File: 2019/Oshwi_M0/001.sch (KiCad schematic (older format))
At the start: 101 parts, among them CN1 MICROSD, CN2 MicroB USB, IC1 APX803, J1 Conn_01x01, J10 Conn_01x01, J11 Conn_01x01, J12 Conn_01x01, J13 Conn_01x01, J14 Conn_01x01, J15 Conn_01x01, J16 Conn_01x01, J17 Conn_01x01, J18 Conn_01x01, J19 Conn_01x01, J2 Conn_01x01, J20 Conn_01x01, J21 Conn_01x01, J22 Conn_01x01, J23 Conn_01x01, J24 USB_MICRO, J26 Micro_SD_Card_Det, J3 Conn_01x01, J4 Conn_01x01, J5 Conn_01x01, J6 Conn_01x01, J7 Conn_01x01, J8 Conn_01x01, J9 Conn_01x01, Q1 MMBT2222, Q2 mmbt2222, SW1 SW_Push, SW2 EVQQ, SW3 EVQQ, U2 Memory_Flash, U3 ATSAMD21G18A-AUT, U5 DISP_LCD_0.9IN_160X80, U6 AP2112K-3.3, Y1 32.768

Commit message: Auto stash before merge of "master" and "origin/master"
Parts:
- removed 3.3VTAP1, 3V3TAP1, GND3TAP1, GNDTAP1, GNDTAP2, VCC1: SEWTAP-ALLIGATOR, Adafruit Circuit Playground Express:SEWALLI, symbol 001-rescue:SEWTAP-ALLIGATOR-Adafruit_Circuit_Playground_Express-eagle-import
- removed BATT1: 3-6VDC, Adafruit Circuit Playground Express:JSTPH2, symbol 001-rescue:CON_JST_PH_2PIN-Adafruit_Circuit_Playground_Express-eagle-import
- removed C11, C13, C14, C15: 1uF, Adafruit Circuit Playground Express:0603-NO, symbol 001-rescue:CAP_CERAMIC0603_NO-Adafruit_Circuit_Playground_Express-eagle-import
- removed C12, C8: 10uF, Adafruit Circuit Playground Express:0805-NO, symbol 001-rescue:CAP_CERAMIC0805-NOOUTLINE-Adafruit_Circuit_Playground_Express-eagle-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
- removed CN1: MICROSD, Adafruit 0.96in 160x80 TFT Display:MICROSD, symbol Adafruit_0.96in_160x80_TFT_Display-eagle-import:MICROSD
- removed CN2: MicroB USB, Adafruit Circuit Playground Express:4UCONN_20329_V2, symbol 001-rescue:USB_MICRO_20329_V2-Adafruit_Circuit_Playground_Express-eagle-import
- removed D4, D5: MBR120, Adafruit Circuit Playground Express:SOD-123, symbol 001-rescue:DIODESOD-123-Adafruit_Circuit_Playground_Express-eagle-import
- removed F1: 6V+ 500mA, Adafruit Circuit Playground Express:R1206, symbol 001-rescue:PTCFUSE-1206-Adafruit_Circuit_Playground_Express-eagle-import
- removed J26: Micro_SD_Card_Det, symbol 001-rescue:Micro_SD_Card_Det-conn
- removed U6: AP2112K-3.3, Adafruit Circuit Playground Express:SOT23-5, symbol 001-rescue:VREG_SOT23-5-Adafruit_Circuit_Playground_Express-eagle-import
- added X?: MICROSD, symbol oshwi_M0:MICROSD
- C? (x3): symbol device:C_Small -> 001-rescue:C_Small-device
- F2: symbol device:Polyfuse_Small -> 001-rescue:Polyfuse_Small-device
- J?: symbol conn:CONN_01X02 -> 001-rescue:CONN_01X02-conn
- R2, R6, R?: symbol device:R_Small -> 001-rescue:R_Small-device
- U?: symbol regul:AP2127K-3.3 -> 001-rescue:AP2127K-3.3-regul
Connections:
- wire segments 287 -> 247
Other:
- note removed: "3.3V Reg"
- note removed: "JST Battery In"
- note removed: "POWER SUPPLY"
- note removed: "USB Power/Data"

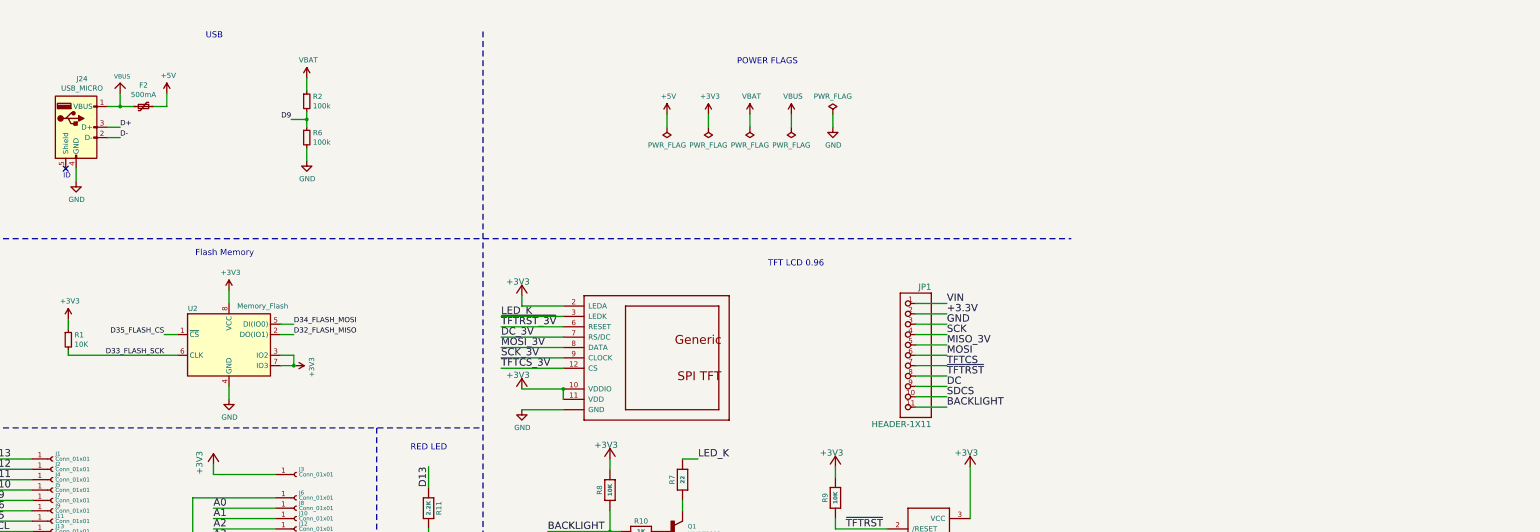
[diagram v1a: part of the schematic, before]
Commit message: Update Symbol MicroUSB
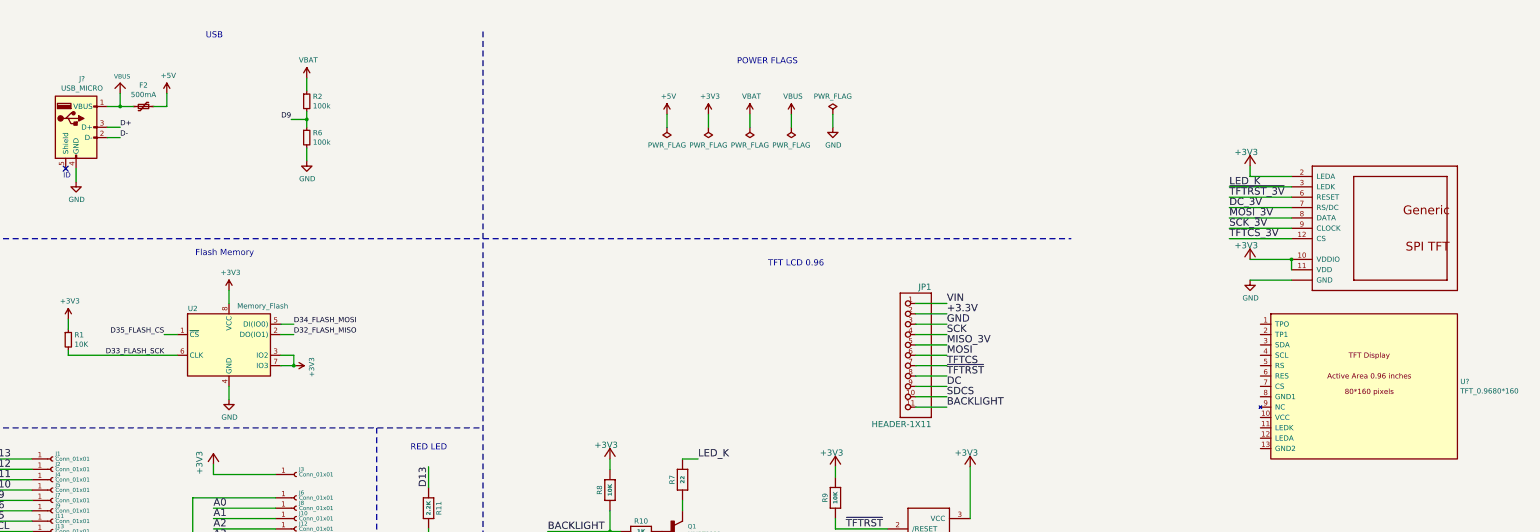
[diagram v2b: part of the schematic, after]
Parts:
- removed J24: USB_MICRO, symbol 001-rescue:USB_MICRO-oshwi_M0
- added J?: USB_MICRO, symbol oshwi_M0:USB_MICRO
- added U?: TFT_0.9680*160, symbol tft-shield:TFT_0.9680*160
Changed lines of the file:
@@
 L Adafruit_0.96in_160x80_TFT_Display-eagle-import:DISP_LCD_0.9IN_160X80 U5
 U 1 1 5CCCC118
-P 12725 3875
-F 0 "U5" H 12725 3875 50  0001 C CNN
-F 1 "DISP_LCD_0.9IN_160X80" H 12725 3875 50  0001 C CNN
-F 2 "Adafruit 0.96in 160x80 TFT Display:TFT_0.96IN_160X80" H 12725 3875 50  0001 C CNN
-F 3 "" H 12725 3875 50  0001 C CNN
-	1    12725 3875
+P 19750 2625
+F 0 "U5" H 19750 2625 50  0001 C CNN
+F 1 "DISP_LCD_0.9IN_160X80" H 19750 2625 50  0001 C CNN
+F 2 "Adafruit 0.96in 160x80 TFT Display:TFT_0.96IN_160X80" H 19750 2625 50  0001 C CNN
+F 3 "" H 19750 2625 50  0001 C CNN
+	1    19750 2625
 	1    0    0    -1
 $EndComp
@@
 Wire Wire Line
 	13325 7850 12425 7850
-Text Label 11025 3775 0    70   ~ 0
+Text Label 18050 2525 0    70   ~ 0
 MOSI_3V
 Wire Wire Line
-	11025 3775 11625 3775
+	18050 2525 18650 2525
 Text Label 12425 7650 0    70   ~ 0
 MOSI
@@
 Wire Wire Line
 	12775 5250 12775 5350
-Text Label 11025 3475 0    70   ~ 0
+Text Label 18050 2225 0    70   ~ 0
 LED_K
 Wire Wire Line
-	11625 3475 11025 3475
+	18650 2225 18050 2225
 Text Label 15325 4250 0    70   ~ 0
 SDCS
 Text Label 15325 3350 0    70   ~ 0
 VIN
-Text Label 11025 3675 0    70   ~ 0
+Text Label 18050 2425 0    70   ~ 0
 DC_3V
 Wire Wire Line
-	11625 3675 11025 3675
-Text Label 11025 3575 0    70   ~ 0
+	18650 2425 18050 2425
+Text Label 18050 2325 0    70   ~ 0
 ~TFTRST_3V
 Wire Wire Line
-	11625 3575 11025 3575
-Text Label 11025 3875 0    70   ~ 0
+	18650 2325 18050 2325
+Text Label 18050 2625 0    70   ~ 0
 SCK_3V
 Wire Wire Line
-	11625 3875 11025 3875
+	18650 2625 18050 2625
 Text Label 12425 7750 0    70   ~ 0
 SCK
@@
 Text Label 15325 3650 0    70   ~ 0
 SCK
-Text Label 11025 3975 0    70   ~ 0
+Text Label 18050 2725 0    70   ~ 0
 TFTCS_3V
 Wire Wire Line
-	11025 3975 11625 3975
+	18050 2725 18650 2725
 Text Label 15325 3450 0    70   ~ 0
 +3.3V
@@
 	13325 8250 12925 8250
 Wire Wire Line
-	11225 3375 11225 3275
-Wire Wire Line
-	11625 3375 11225 3375
-Connection ~ 11625 4175
-Wire Wire Line
-	11625 4275 11625 4175
-Wire Wire Line
-	11225 4175 11625 4175
+	18250 2125 18250 2025
+Wire Wire Line
+	18650 2125 18250 2125
+Connection ~ 18650 2925
+Wire Wire Line
+	18650 3025 18650 2925
+Wire Wire Line
+	18250 2925 18650 2925
 Wire Wire Line
 	15550 5425 15550 4925
@@
 	13325 8350 13225 8350
 Wire Wire Line
-	11225 4375 11625 4375
+	18250 3125 18650 3125
 Wire Wire Line
 	15550 5625 15550 5725
@@
 L 001-rescue:+3V3-Adafruit_Feather_M0_Express-eagle-import #+3V06
 U 1 1 5CC64777
-P 11225 3175
-F 0 "#+3V06" H 11225 3175 50  0001 C CNN
-F 1 "+3V3" H 11075 3175 59  0000 L BNN
-F 2 "" H 11225 3175 50  0001 C CNN
-F 3 "" H 11225 3175 50  0001 C CNN
-	1    11225 3175
+P 18250 1925
+F 0 "#+3V06" H 18250 1925 50  0001 C CNN
+F 1 "+3V3" H 18100 1925 59  0000 L BNN
+F 2 "" H 18250 1925 50  0001 C CNN
+F 3 "" H 18250 1925 50  0001 C CNN
+	1    18250 1925
 	1    0    0    -1
 $EndComp
@@
 L 001-rescue:+3V3-Adafruit_Feather_M0_Express-eagle-import #+3V09
 U 1 1 5CC7148B
-P 11225 4075
-F 0 "#+3V09" H 11225 4075 50  0001 C CNN
-F 1 "+3V3" H 11075 4075 59  0000 L BNN
-F 2 "" H 11225 4075 50  0001 C CNN
-F 3 "" H 11225 4075 50  0001 C CNN
-	1    11225 4075
+P 18250 2825
+F 0 "#+3V09" H 18250 2825 50  0001 C CNN
+F 1 "+3V3" H 18100 2825 59  0000 L BNN
+F 2 "" H 18250 2825 50  0001 C CNN
+F 3 "" H 18250 2825 50  0001 C CNN
+	1    18250 2825
 	1    0    0    -1
 $EndComp
@@
 L power:GND #PWR019
 U 1 1 5CE5E5EC
-P 11225 4375
-F 0 "#PWR019" H 11225 4125 50  0001 C CNN
-F 1 "GND" H 11230 4202 50  0000 C CNN
-F 2 "" H 11225 4375 50  0001 C CNN
-F 3 "" H 11225 4375 50  0001 C CNN
-	1    11225 4375
+P 18250 3125
+F 0 "#PWR019" H 18250 2875 50  0001 C CNN
+F 1 "GND" H 18255 2952 50  0000 C CNN
+F 2 "" H 18250 3125 50  0001 C CNN
+F 3 "" H 18250 3125 50  0001 C CNN
+	1    18250 3125
 	1    0    0    -1
 $EndComp
@@
 	1    0    0    -1
 $EndComp
-$Comp
-L 001-rescue:USB_MICRO-oshwi_M0 J24
-U 1 1 5CF4E9B6
-P 6925 1650
-F 0 "J24" H 6982 2117 50  0000 C CNN
-F 1 "USB_MICRO" H 6982 2026 50  0000 C CNN
-F 2 "" H 7075 1600 50  0001 C CNN
-F 3 "" H 7075 1600 50  0001 C CNN
-	1    6925 1650
-	1    0    0    -1
-$EndComp
 Wire Wire Line
 	7225 1650 7350 1650
@@
 	1    0    0    -1
 $EndComp
+$Comp
+L oshwi_M0:USB_MICRO J?
+U 1 1 5CF00609
+P 6925 1650
+F 0 "J?" H 6982 2117 50  0000 C CNN
+F 1 "USB_MICRO" H 6982 2026 50  0000 C CNN
+F 2 "" H 7075 1600 50  0001 C CNN
+F 3 "" H 7075 1600 50  0001 C CNN
+	1    6925 1650
+	1    0    0    -1
+$EndComp
+$Comp
+L tft-shield:TFT_0.9680*160 U?
+U 1 1 5CEFFB80
+P 19400 4150
+F 0 "U?" H 20278 4196 50  0000 L CNN
+F 1 "TFT_0.9680*160" H 20278 4105 50  0000 L CNN
+F 2 "" H 19400 4150 50  0001 C CNN
+F 3 "" H 19400 4150 50  0001 C CNN
+	1    19400 4150
+	1    0    0    -1
+$EndComp

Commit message: Add Changes to Oshwi 2019 Badge
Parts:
- removed D2, IO1, IO2, IO3, RX1, SCL1, SDA1, TX1: SEWTAP-ALLIGATOR, Adafruit Circuit Playground Express:SEWALLI, symbol 001-rescue:SEWTAP-ALLIGATOR-Adafruit_Circuit_Playground_Express-eagle-import
- removed D3: IR TX, Adafruit Circuit Playground Express:CHIPLED_1206_NOOUTLINE, symbol 001-rescue:LED1206_NOOUTLINE-Adafruit_Circuit_Playground_Express-eagle-import
- removed IC1: APX803, Adafruit 0.96in 160x80 TFT Display:SOT23, symbol Adafruit_0.96in_160x80_TFT_Display-eagle-import:AXP083-SAG
- removed J1, J10, J11, J12, J13, J14, J15, J16, J17, J18, J19, J2, J20, J21, J22, J23, J3, J4, J5, J6, J7, J8, J9: Conn_01x01, OSHwi:CONN-HEADER-STRAIGHT-P2.54MM-1x01, symbol 001-rescue:Conn_01x01_Female-Connector
- removed JP1: HEADER-1X11, Adafruit 0.96in 160x80 TFT Display:1X11_ROUND, symbol Adafruit_0.96in_160x80_TFT_Display-eagle-import:HEADER-1X11
- removed L1: RED, OSHwi:LED_0805, symbol 001-rescue:LED-Device
- removed L2: RED, Adafruit Circuit Playground Express:CHIPLED_0805_NOOUTLINE, symbol 001-rescue:LED0805_NOOUTLINE-Adafruit_Circuit_Playground_Express-eagle-import
- removed PWR1: GREEN, Adafruit Circuit Playground Express:CHIPLED_0805_NOOUTLINE, symbol 001-rescue:LED0805_NOOUTLINE-Adafruit_Circuit_Playground_Express-eagle-import
- removed Q1: MMBT2222, Adafruit 0.96in 160x80 TFT Display:SOT23-WIDE, symbol Adafruit_0.96in_160x80_TFT_Display-eagle-import:TRANSISTOR_NPNWIDE
- removed Q2: mmbt2222, Adafruit Circuit Playground Express:SOT23-R, symbol 001-rescue:TRANSISTOR_NPN-Adafruit_Circuit_Playground_Express-eagle-import
- removed R10: 1K, Adafruit 0.96in 160x80 TFT Display:0603-NO, symbol Adafruit_0.96in_160x80_TFT_Display-eagle-import:RESISTOR_0603_NOOUT
- removed R11: 2.2K, OSHwi:R_0805_HandSoldering, symbol 001-rescue:RESISTOR_0603_NOOUT-Adafruit_Feather_M0_Express-eagle-import
- removed R12: 100, Adafruit Circuit Playground Express:0603-NO, symbol 001-rescue:RESISTOR_0603_NOOUT-Adafruit_Circuit_Playground_Express-eagle-import
- removed R4, R5: 1K, Adafruit Circuit Playground Express:0603-NO, symbol 001-rescue:RESISTOR_0603_NOOUT-Adafruit_Circuit_Playground_Express-eagle-import
- removed R7: 22, Adafruit 0.96in 160x80 TFT Display:0603-NO, symbol Adafruit_0.96in_160x80_TFT_Display-eagle-import:RESISTOR_0603_NOOUT
- removed R8, R9: 10K, Adafruit 0.96in 160x80 TFT Display:0603-NO, symbol Adafruit_0.96in_160x80_TFT_Display-eagle-import:RESISTOR_0603_NOOUT
- removed RESET1: KMR2, Adafruit Circuit Playground Express:BTN_KMR2_4.6X2.8, symbol 001-rescue:SWITCH_TACT_SMT4.6X2.8-Adafruit_Circuit_Playground_Express-eagle-imp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
- removed SW2, SW3: EVQQ, Adafruit Circuit Playground Express:EVQ-Q2_SMALLER, symbol 001-rescue:SWITCH_TACT_SMT_EVQQ2_SMALL-Adafruit_Circuit_Playground_Express-eagl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
- removed SWITCH1: EG1390, Adafruit Circuit Playground Express:EG1390, symbol 001-rescue:DPDT-EG1390-Adafruit_Circuit_Playground_Express-eagle-import
- removed U5: DISP_LCD_0.9IN_160X80, Adafruit 0.96in 160x80 TFT Display:TFT_0.96IN_160X80, symbol Adafruit_0.96in_160x80_TFT_Display-eagle-import:DISP_LCD_0.9IN_160X80
- added C8: 1uF, symbol Device:C_Small
- added D3: RED, symbol Device:LED_Small
- added D4: GREEN, symbol Device:LED_Small
- added J26: Conn_01x08_Male, symbol Connector:Conn_01x08_Male
- added Q1: BJT-NPN-40V-0.6A-MMBT2222, Wickerlib:SOT-23-3, symbol wickerlib:BJT-NPN-40V-0.6A-MMBT2222
- added R10: 10 K, symbol Device:R_Small
- added R4, R5: R_Small, symbol Device:R_Small
- added R7: 10 ohm, symbol Device:R_Small
- added R8: 1K, symbol Device:R_Small
- added S1: SPST, Wickerlib:SWITCH-OMRON-MOMENTARY-SMD-B3U-1000P, symbol wickerlib:SWITCH-MOMENT-SPST-NO-0.05A-12V-SMT-B3U-1000P
- gave numbers to parts that had none: 10
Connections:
- net labels added: *D4_LEFTBUTTON, *D5_RIGHTBUTTON, BLK, LEDK, TFT_CS, TFT_DC, TFT_RES, TFT_SCL, TFT_SDA
- net labels removed: 3.3V, A0, A1, A2, A3, A4, A5, BACKLIGHT, D0, D1, D10, D11, D12, D13, D4_LEFTBUTTON, D5, D5_RIGHTBUTTON, D6, DC, DC_3V, LED_K, MISO_3V, MOSI_3V, SCK_3V, SCL, SDA, SDCS, TFTCS, TFTCS_3V, VCC, VIN, ~TFTRST, ~TFTRST_3V
- wire segments 247 -> 186
- no-connect marks 12 -> 14
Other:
- note added: "*Capacitive Touch/IO Pads"
- note added: "*D4_LEFTBUTTON\n*D5_RIGHTBUTTON\n*Slide Switch"
- note removed: "BREAKOUTS"
- note removed: "Capacitive Touch/IO Pads"
- note removed: "RED LED"
- note removed: "Slide Switch"
- note removed: "Tact Switch"
- moved on the sheet: C10, C2, C3, C4, C5, C6, D1, J25, R1, R3, SW1, U1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

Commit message: Add changes tft_shield
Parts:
- J26: footprint (none) -> Oshwi_M0:TFT_0.96IN_160X80
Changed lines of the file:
@@
 F 0 "J26" H 11733 4256 50  0000 C CNN
 F 1 "Conn_01x08_Male" H 11733 4165 50  0000 C CNN
-F 2 "" H 11625 3775 50  0001 C CNN
+F 2 "Oshwi_M0:TFT_0.96IN_160X80" H 11625 3775 50  0001 C CNN
 F 3 "~" H 11625 3775 50  0001 C CNN
 	1    11625 3775
